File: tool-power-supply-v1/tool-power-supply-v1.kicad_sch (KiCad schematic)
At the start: 0 parts

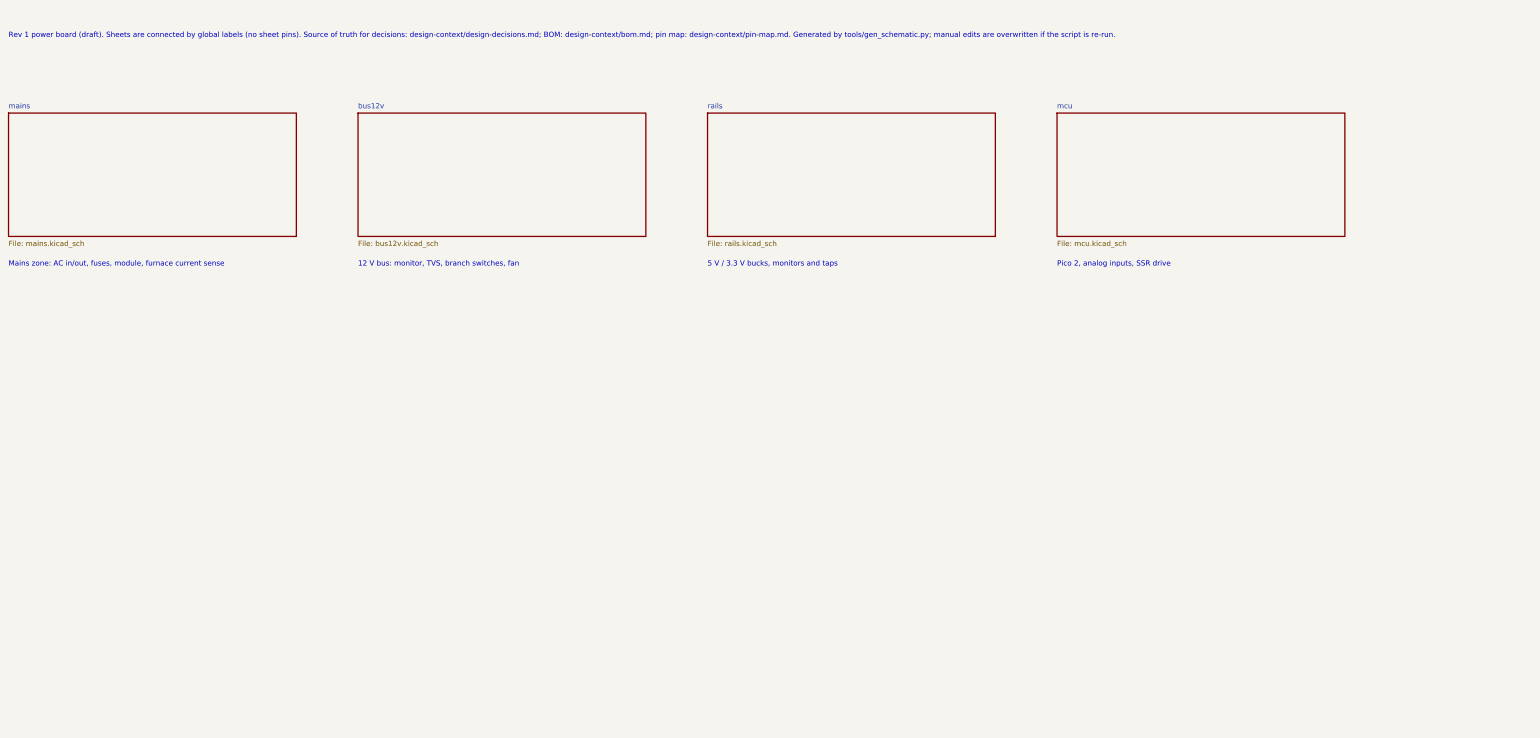
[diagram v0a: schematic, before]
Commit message: schematic update: cleaned up by using sheet labels and busses, updated documentation
Co-Authored-By: Claude Sonnet 5.5 <noreply@anthropic.com>
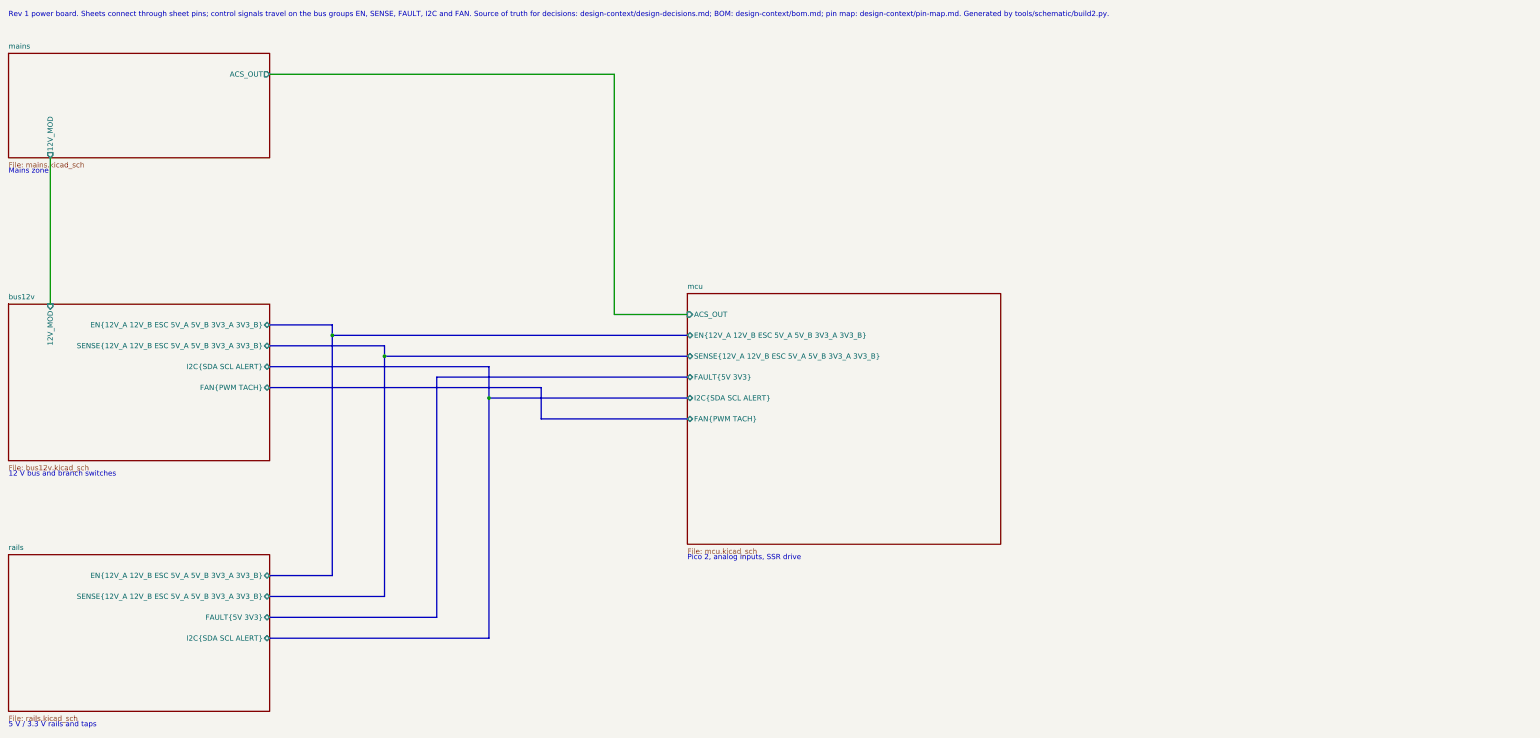
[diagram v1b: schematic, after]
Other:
- sheet bus12v ports: added 12V_MOD, EN{12V_A 12V_B ESC 5V_A 5V_B 3V3_A 3V3_B}, FAN{PWM TACH}, I2C{SDA SCL ALERT}, SENSE{12V_A 12V_B ESC 5V_A 5V_B 3V3_A 3V3_B}; removed none
- sheet mains ports: added 12V_MOD, ACS_OUT; removed none
- sheet mcu ports: added ACS_OUT, EN{12V_A 12V_B ESC 5V_A 5V_B 3V3_A 3V3_B}, FAN{PWM TACH}, FAULT{5V 3V3}, I2C{SDA SCL ALERT}, SENSE{12V_A 12V_B ESC 5V_A 5V_B 3V3_A 3V3_B}; removed none
- sheet rails ports: added EN{12V_A 12V_B ESC 5V_A 5V_B 3V3_A 3V3_B}, FAULT{5V 3V3}, I2C{SDA SCL ALERT}, SENSE{12V_A 12V_B ESC 5V_A 5V_B 3V3_A 3V3_B}; removed none
- note added: "12 V bus and branch switches"
- note added: "5 V / 3.3 V rails and taps"
- note added: "Mains zone"
- note added: "Rev 1 power board. Sheets connect through sheet pins; control signals travel on the bus groups EN, SENSE, FAULT, I2C and FAN. Source of truth for decisions: design-context/design-decisions.md; BOM: design-context/bom.md; pin map: design-context/pin-map.md. Generated by tools/schematic/build2.py."
- note removed: "12 V bus: monitor, TVS, branch switches, fan"
- note removed: "5 V / 3.3 V bucks, monitors and taps"
- note removed: "Mains zone: AC in/out, fuses, module, furnace current sense"
- note removed: "Rev 1 power board (draft). Sheets are connected by global labels (no sheet pins). Source of truth for decisions: design-context/design-decisions.md; BOM: design-context/bom.md; pin map: design-context/pin-map.md. Generated by tools/gen_schematic.py; manual edits are overwritten if the script is re-run."
